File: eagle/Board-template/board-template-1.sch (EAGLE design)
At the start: 1 part

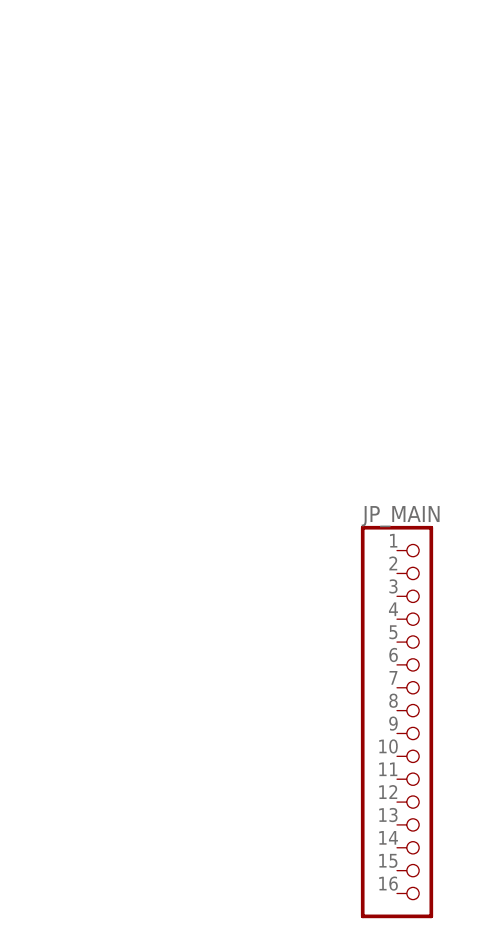
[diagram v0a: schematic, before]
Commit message: eagle merge template board with h-br
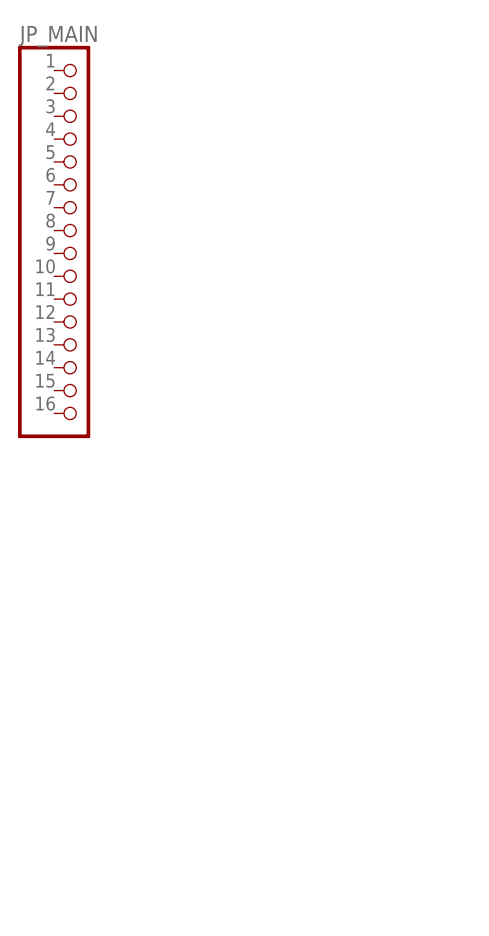
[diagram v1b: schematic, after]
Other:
- moved on the sheet: JP_MAIN
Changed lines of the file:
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@@
 <setting verticaltext="up"/>
 </settings>
-<grid distance="0.1" unitdist="inch" unit="inch" style="lines" multiple="1" display="yes" altdistance="0.01" altunitdist="inch" altunit="inch"/>
+<grid distance="0.1" unitdist="inch" unit="inch" style="lines" multiple="1" display="no" altdistance="0.01" altunitdist="inch" altunit="inch"/>
 <layers>
 <layer number="1" name="Top" color="4" fill="1" visible="no" active="no"/>
@@
 </plain>
 <instances>
-<instance part="JP_MAIN" gate="A" x="12.7" y="50.8"/>
+<instance part="JP_MAIN" gate="A" x="-25.4" y="104.14"/>
 </instances>
 <busses>
